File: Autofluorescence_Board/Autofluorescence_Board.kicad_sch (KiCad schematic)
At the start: 19 parts, among them J3 Conn_01x02, J4 Conn_01x04, J5 Conn_01x02, Q1 A03401A, Q2 BSS138, U2 PAM2863ECR

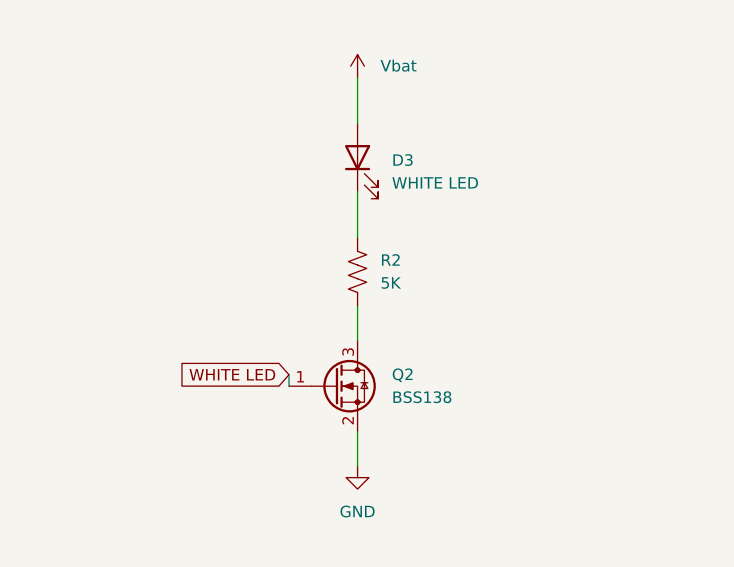
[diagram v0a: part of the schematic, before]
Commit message: switching 5k for standard 5.1k resistor
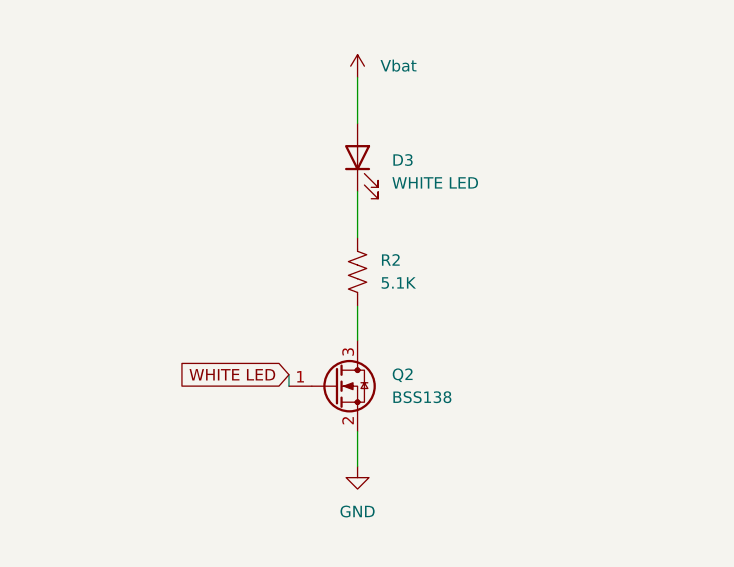
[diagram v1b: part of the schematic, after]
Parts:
- R2: value 5K -> 5.1K
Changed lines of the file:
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@@
 			)
 		)
-		(property "Value" "5K"
+		(property "Value" "5.1K"
 			(at 238.76 92.7099 0)
 			(show_name no)

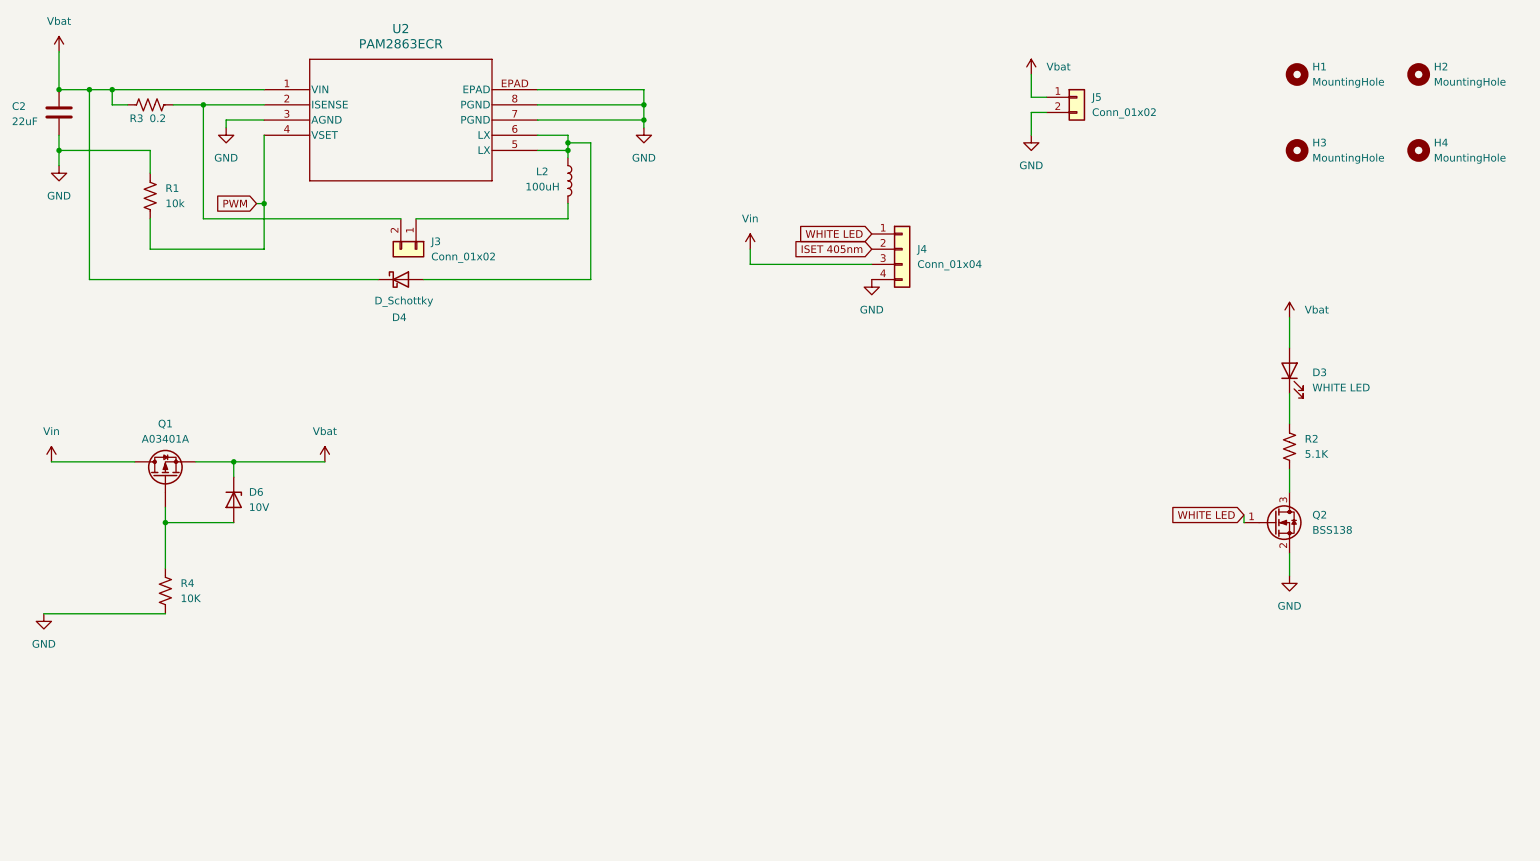
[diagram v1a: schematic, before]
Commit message: Fixed up schematic, some footprints still need fixing
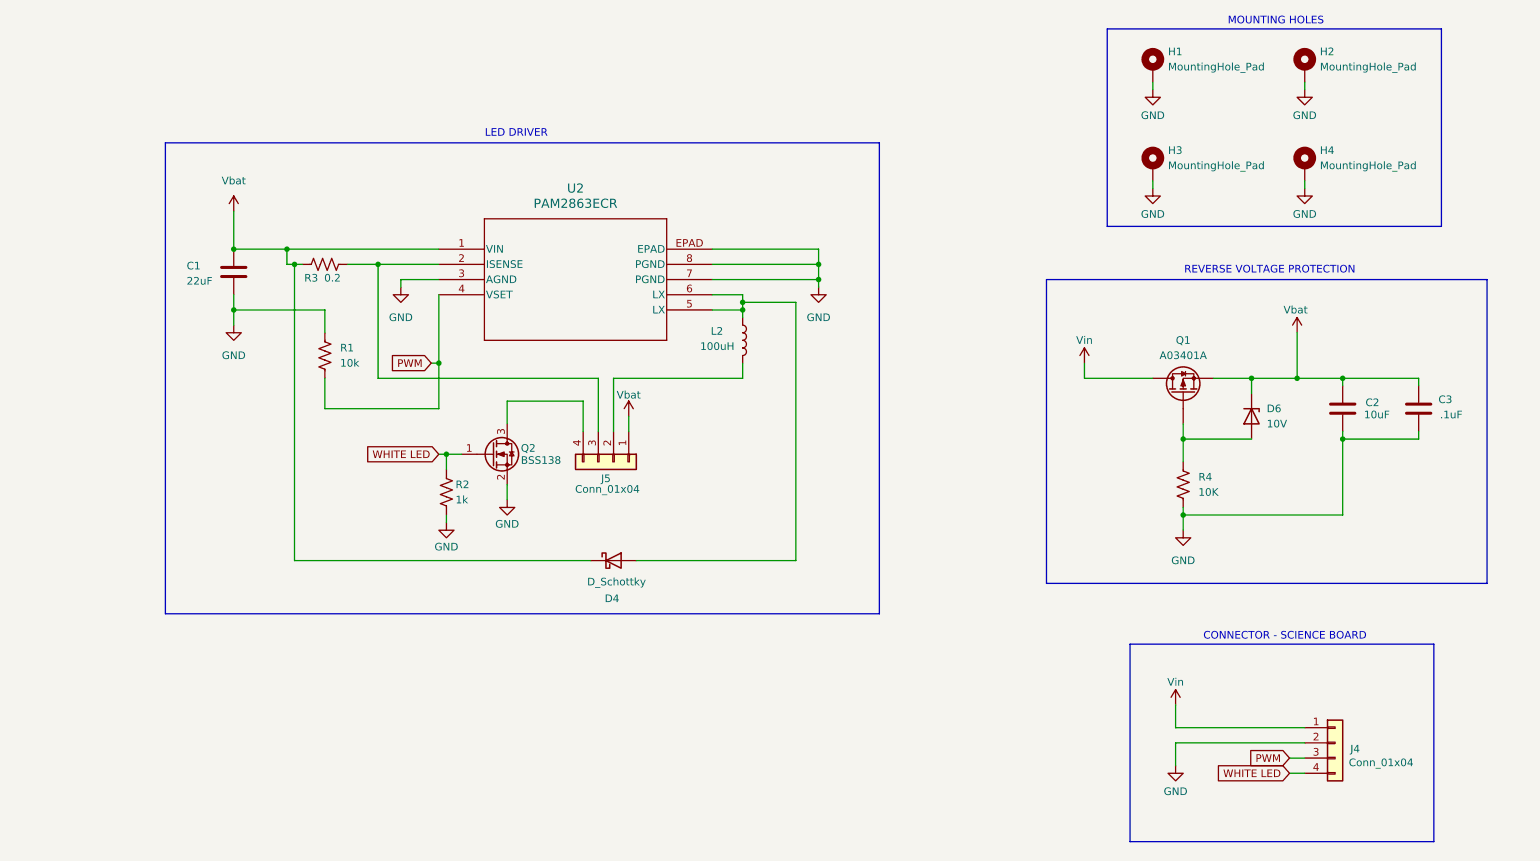
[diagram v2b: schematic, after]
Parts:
- removed D3: WHITE LED, Diode_SMD:D_0603_1608Metric_Pad1.05x0.95mm_HandSolder, symbol Device:LED
- removed H1, H2, H3, H4: MountingHole, symbol Mechanical:MountingHole
- removed J3, J5: Conn_01x02, Connector_JST:JST_PH_B2B-PH-K_1x02_P2.00mm_Vertical, symbol Connector_Generic:Conn_01x02
- added C2: 10uF, Capacitor_SMD:C_0603_1608Metric_Pad1.08x0.95mm_HandSolder, symbol Device:C
- added C3: .1uF, Capacitor_SMD:C_0603_1608Metric_Pad1.08x0.95mm_HandSolder, symbol Device:C
- added H1, H2, H3, H4: MountingHole_Pad, MRDT_Drill_Holes:4_40_Hole_Pad_Via, symbol Mechanical:MountingHole_Pad
- added J5: Conn_01x04, Connector_JST:JST_PH_S4B-PH-K_1x04_P2.00mm_Horizontal, symbol Connector_Generic:Conn_01x04
- L2: footprint Inductor_SMD:L_0201_0603Metric_Pad0.64x0.40mm_HandSolder -> AF_Footprint:DR73
- R2: value 5.1K -> 1k
- renumbered C2 to C1
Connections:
- net ISET 405nm is gone; now on net GND: J4.2 (Pin_2)
- net GND: now also R2.2, C2.2, C3.2, H1.1, H2.1, H3.1, H4.1; no longer J4.4 (Pin_4)
- net PWM: now also J4.3 (Pin_3)
- net Vbat: now also C2.1, C3.1, J5.1 (Pin_1)
- net Vin: now also J4.1 (Pin_1); no longer J4.3 (Pin_3)
- net WHITE LED: now also J4.4 (Pin_4), R2.1; no longer J4.1 (Pin_1)
- net at R3.2, U2.2 (ISENSE): now also J5.3 (Pin_3)
- net at L2.2: now also J5.2 (Pin_2)
- net at Q2.3 (D): now also J5.4 (Pin_4); no longer R2.2
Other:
- note added: "CONNECTOR - SCIENCE BOARD"
- note added: "LED DRIVER"
- note added: "MOUNTING HOLES"
- note added: "REVERSE VOLTAGE PROTECTION"
- moved on the sheet: C1, D4, D6, J4, L2, Q1, Q2, R1, R3, R4, U2

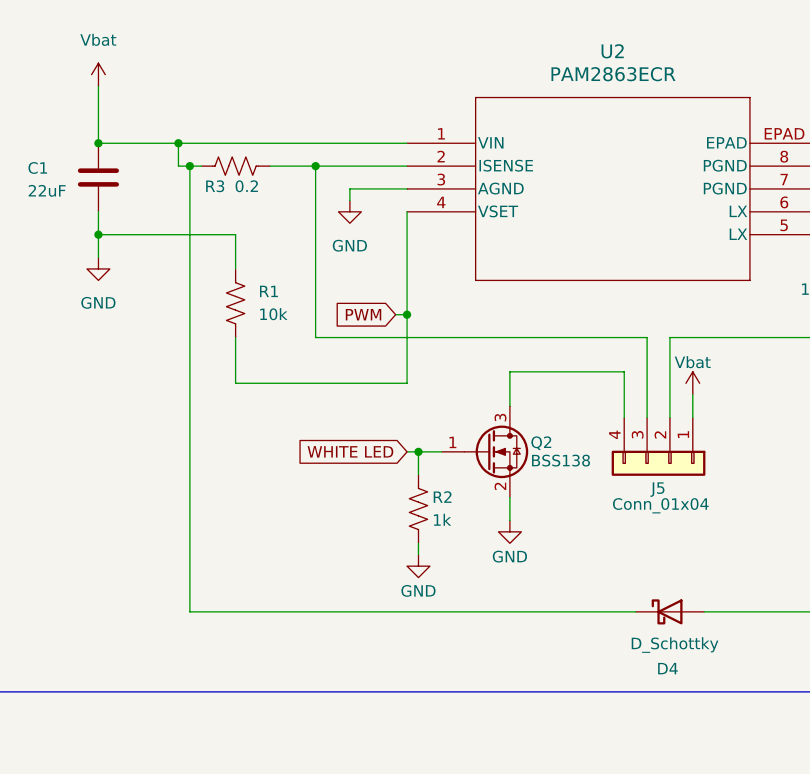
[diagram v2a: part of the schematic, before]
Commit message: Add Resistor Values
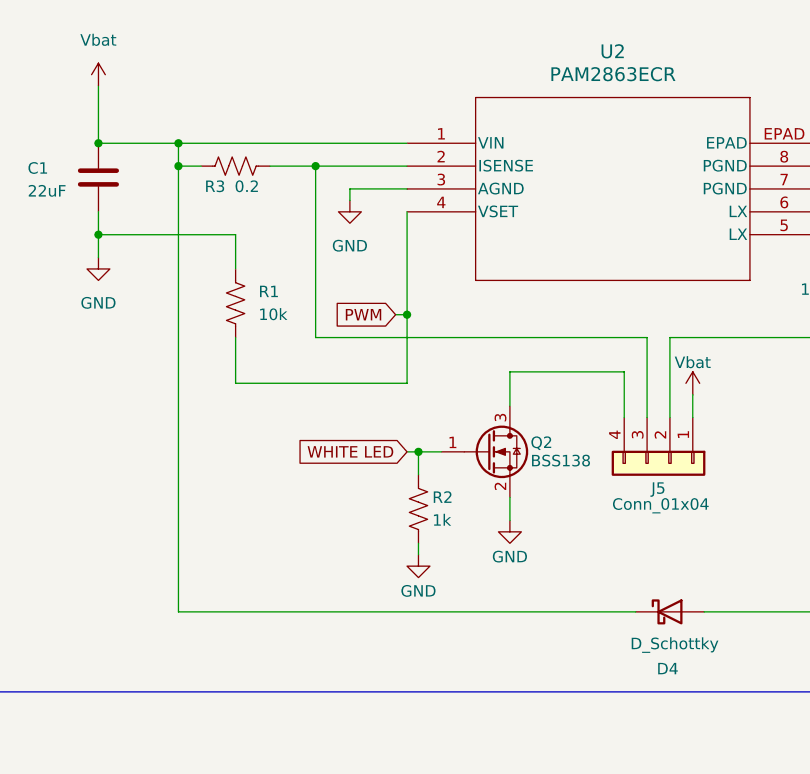
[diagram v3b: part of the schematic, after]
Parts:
- R3: footprint Resistor_SMD:R_0603_1608Metric_Pad0.98x0.95mm_HandSolder -> Resistor_SMD:R_0805_2012Metric_Pad1.20x1.40mm_HandSolder

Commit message: Fixed footprints
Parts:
- C1: footprint Capacitor_SMD:C_0603_1608Metric_Pad1.08x0.95mm_HandSolder -> Capacitor_SMD:C_1206_3216Metric_Pad1.33x1.80mm_HandSolder
- D1: renamed from D4; footprint Diode_SMD:D_SOD-123 -> Diode_SMD:D_SOD-123F
- D2: renamed from D6; footprint Package_DIP:DIP-40_W15.24mm -> MRDT_Devices:SOD-123_ONS-L
- R1: footprint Package_DIP:DIP-8_W7.62mm -> Resistor_SMD:R_0603_1608Metric_Pad0.98x0.95mm_HandSolder
- renumbered J5 to J1, J4 to J2, L2 to L1, Q2 to Q1, Q1 to Q2
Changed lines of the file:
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@@
 		(dnp no)
 		(fields_autoplaced yes)
-		(property "Reference" "D6"
+		(property "Reference" "D2"
 			(at 232.41 85.0899 90)
 			(show_name no)
@@
 			)
 		)
-		(property "Footprint" "Package_DIP:DIP-40_W15.24mm"
+		(property "Footprint" "MRDT_Devices:SOD-123_ONS-L"
 			(at 229.87 86.36 0)
 			(hide yes)
@@
 			(project "Autofluorescence_Board"
 				(path "/72deb9c7-3e3f-41e9-884c-65f2f5e1cc20"
-					(reference "D6")
+					(reference "D2")
 					(unit 1)
 				)
@@
 		(in_pos_files yes)
 		(dnp no)
-		(property "Reference" "J4"
+		(property "Reference" "J2"
 			(at 246.38 141.986 0)
 			(show_name no)
@@
 			(project "Autofluorescence_Board"
 				(path "/72deb9c7-3e3f-41e9-884c-65f2f5e1cc20"
-					(reference "J4")
+					(reference "J2")
 					(unit 1)
 				)
@@
 		(in_pos_files yes)
 		(dnp no)
-		(property "Reference" "D4"
+		(property "Reference" "D1"
 			(at 122.936 116.84 0)
 			(show_name no)
@@
 			)
 		)
-		(property "Footprint" "Diode_SMD:D_SOD-123"
+		(property "Footprint" "Diode_SMD:D_SOD-123F"
 			(at 123.19 110.49 0)
 			(hide yes)
@@
 			)
 		)
-		(property "Datasheet" "https://www.digikey.com/en/products/detail/avx-corporation/SD0603S040S0R2/478-7798-1-ND/3749483"
+		(property "Datasheet" "https://www.digikey.com/en/products/detail/smc-diode-solutions/DSS14U/8341859"
 			(at 123.19 110.49 0)
 			(hide yes)
@@
 			(project "Autofluorescence_Board"
 				(path "/72deb9c7-3e3f-41e9-884c-65f2f5e1cc20"
-					(reference "D4")
+					(reference "D1")
 					(unit 1)
 				)
@@
 			)
 		)
-		(property "Footprint" "Package_DIP:DIP-8_W7.62mm"
+		(property "Footprint" "Resistor_SMD:R_0603_1608Metric_Pad0.98x0.95mm_HandSolder"
 			(at 73.914 75.946 90)
 			(hide yes)
@@
 			)
 		)
-		(property "Datasheet" ""
+		(property "Datasheet" "https://www.digikey.com/en/products/detail/rohm-semiconductor/ESR03EZPF1002/RHM10KADCT-ND/1983753"
 			(at 74.93 76.2 0)
 			(hide yes)
@@
 		(in_pos_files yes)
 		(dnp no)
-		(property "Reference" "J5"
+		(property "Reference" "J1"
 			(at 121.92 96.774 90)
 			(show_name no)
@@
 			(project "Autofluorescence_Board"
 				(path "/72deb9c7-3e3f-41e9-884c-65f2f5e1cc20"
-					(reference "J5")
+					(reference "J1")
 					(unit 1)
 				)
@@
 		(in_pos_files yes)
 		(dnp no)
-		(property "Reference" "Q2"
+		(property "Reference" "Q1"
 			(at 107.696 91.694 0)
 			(show_name no)
@@
 			(project "Autofluorescence_Board"
 				(path "/72deb9c7-3e3f-41e9-884c-65f2f5e1cc20"
-					(reference "Q2")
+					(reference "Q1")
 					(unit 1)
 				)
@@
 		(dnp no)
 		(fields_autoplaced yes)
-		(property "Reference" "Q1"
+		(property "Reference" "Q2"
 			(at 218.44 73.66 90)
 			(show_name no)
@@
 			(project "Autofluorescence_Board"
 				(path "/72deb9c7-3e3f-41e9-884c-65f2f5e1cc20"
-					(reference "Q1")
+					(reference "Q2")
 					(unit 1)
 				)
@@
 			)
 		)
-		(property "Footprint" "Capacitor_SMD:C_0603_1608Metric_Pad1.08x0.95mm_HandSolder"
+		(property "Footprint" "Capacitor_SMD:C_1206_3216Metric_Pad1.33x1.80mm_HandSolder"
 			(at 60.6552 66.04 0)
 			(hide yes)
@@
 			)
 		)
-		(property "Datasheet" ""
+		(property "Datasheet" "www.digikey.com/en/products/detail/cal-chip-electronics-inc/GMC31X5R226M35NT/18151064"
 			(at 59.69 62.23 0)
 			(hide yes)
@@
 		(in_pos_files yes)
 		(dnp no)
-		(property "Reference" "L2"
+		(property "Reference" "L1"
 			(at 139.446 72.136 0)
 			(show_name no)
@@
 			(project "Autofluorescence_Board"
 				(path "/72deb9c7-3e3f-41e9-884c-65f2f5e1cc20"
-					(reference "L2")
-					(unit 1)
-				)
+					(reference "L1")
+					(unit 1)
+				)

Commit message: Imported component into layout!
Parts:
- renumbered U2 to U1
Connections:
- net Vbat: now also Q2.2 (S); no longer Q2.S
- net Vin: now also Q2.3 (D); no longer Q2.D
- net at D2.2 (A), R4.1: now also Q2.1 (G); no longer Q2.G
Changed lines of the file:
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@@
 		(dnp no)
 		(fields_autoplaced yes)
-		(property "Reference" "U2"
+		(property "Reference" "U1"
 			(at 116.84 48.26 0)
 			(show_name no)
@@
 			(project "Autofluorescence_Board"
 				(path "/72deb9c7-3e3f-41e9-884c-65f2f5e1cc20"
-					(reference "U2")
+					(reference "U1")
 					(unit 1)
 				)
@@
 			)
 		)
-		(pin "D"
-		)
-		(pin "G"
-		)
-		(pin "S"
-		)
-		(instances
+		(pin "3"
+		)
+		(pin "1"
+		)
+		(pin "2"
+		)
+		(instances

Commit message: Rearranged Layout
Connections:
- net GND: now also U1.9 (EPAD); no longer U1.EPAD
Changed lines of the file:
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@@
 		)
 		(property "Footprint" "Package_SO:Diodes_SO-8EP"
-			(at 93.98 58.42 0)
+			(at 92.71 53.34 0)
 			(hide yes)
 			(show_name no)
@@
 		)
 		(property "Datasheet" "https://www.mouser.com/en/ProductDetail/Diodes-Incorporated/PAM2863ECR?qs=pYVYkI7xuRXLW6Fe66wa3w%3D%3D&utm_id=10957129881&utm_source=google&utm_medium=cpc&utm_marketing_tactic=amercorp&gad_source=1&gad_campaignid=10957129881&gclid=CjwKCAjwotzWBhBFEiwA1JhPoJ7eXeCP1n9vMRbjtolV1BtqwhTLIWsrRgOsrPQ_K7fSvjvwSt5RshoC8UMQAvD_BwE"
-			(at 93.98 58.42 0)
+			(at 118.364 55.372 0)
 			(hide yes)
 			(show_name no)
@@
 		(pin "7"
 		)
-		(pin "EPAD"
+		(pin "9"
 		)
 		(instances

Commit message: Finalized Initial Layout
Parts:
- J2: footprint Connector_JST:JST_PH_B4B-PH-K_1x04_P2.00mm_Vertical -> Connector_JST:JST_PH_S4B-PH-K_1x04_P2.00mm_Horizontal
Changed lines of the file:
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@@
 			)
 		)
-		(property "Footprint" "Connector_JST:JST_PH_B4B-PH-K_1x04_P2.00mm_Vertical"
+		(property "Footprint" "Connector_JST:JST_PH_S4B-PH-K_1x04_P2.00mm_Horizontal"
 			(at 243.84 140.97 0)
 			(hide yes)

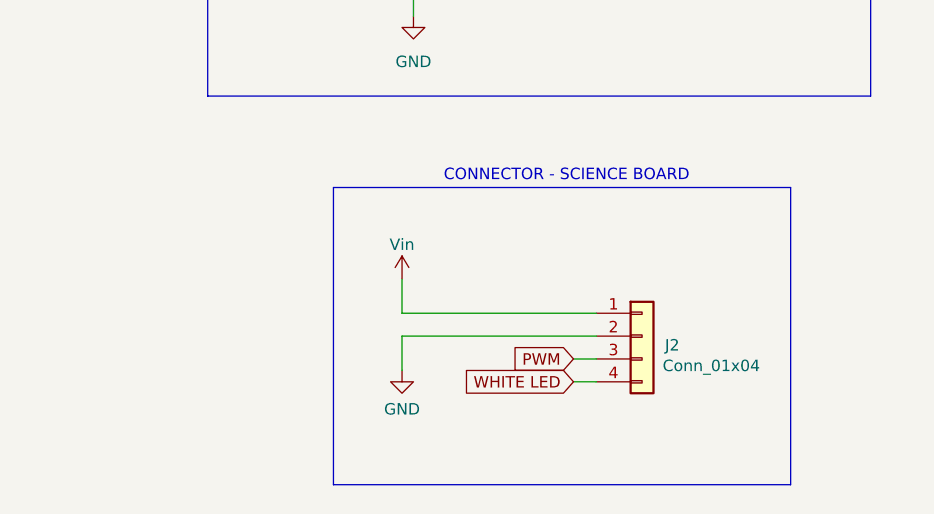
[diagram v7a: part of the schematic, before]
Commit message: added fan connector, cause im a dumbass
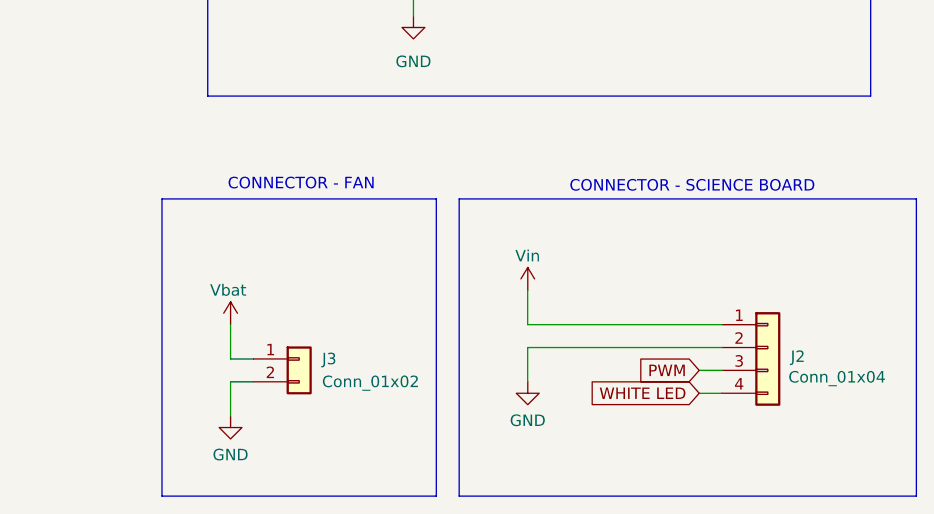
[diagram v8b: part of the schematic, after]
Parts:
- added J3: Conn_01x02, Connector_JST:JST_PH_S2B-PH-K_1x02_P2.00mm_Horizontal, symbol Connector_Generic:Conn_01x02
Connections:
- net GND: now also J3.2 (Pin_2)
- net Vbat: now also J3.1 (Pin_1)
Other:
- note added: "CONNECTOR - FAN"
- moved on the sheet: J2
